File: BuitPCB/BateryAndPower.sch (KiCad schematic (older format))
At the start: 12 parts, among them J13 Conn_01x02, U5 STBC08

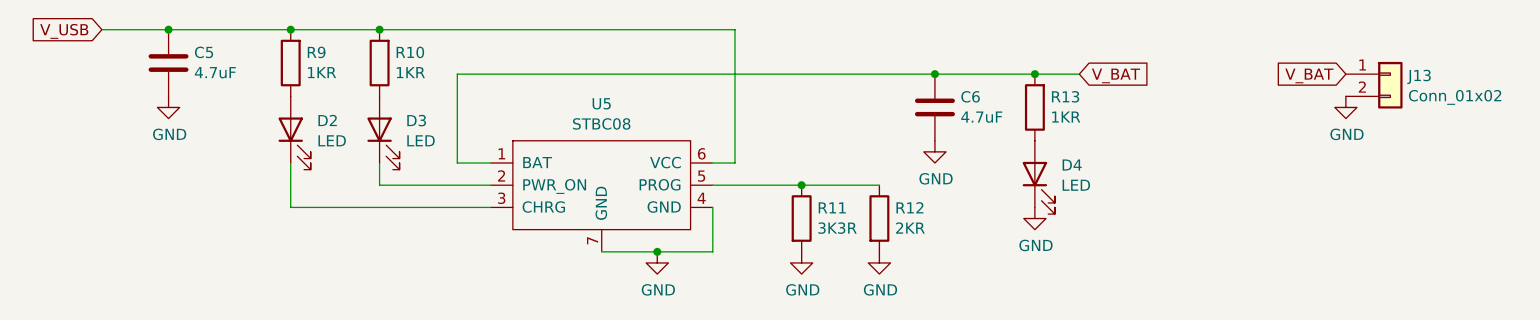
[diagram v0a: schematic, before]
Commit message: Updated adding esp8266 transceiver module
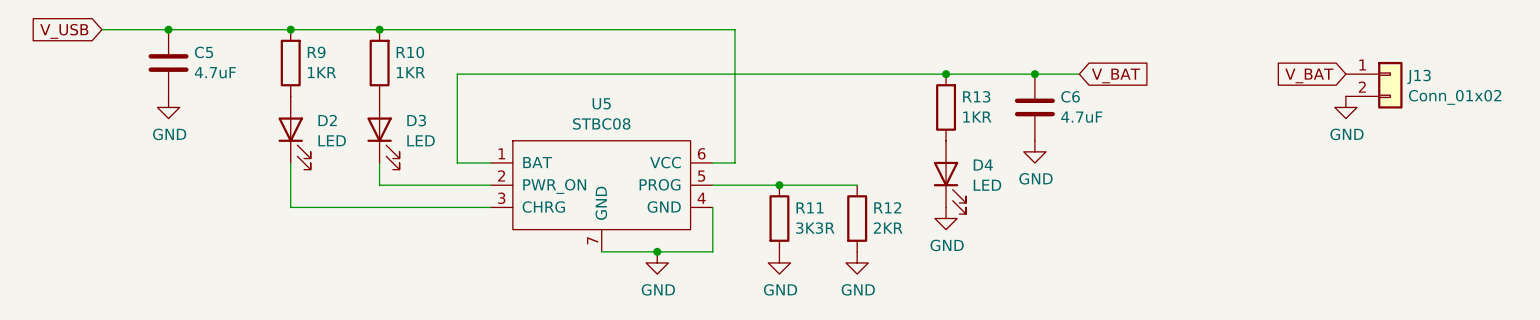
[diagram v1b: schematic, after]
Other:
- moved on the sheet: C6, D4, R11, R12, R13
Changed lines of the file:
@@
 L Device:R R11
 U 1 1 61BB77AB
-P 6600 4050
-F 0 "R11" H 6670 4096 50  0000 L CNN
-F 1 "3K3R" H 6670 4005 50  0000 L CNN
-F 2 "Resistor_SMD:R_0805_2012Metric_Pad1.20x1.40mm_HandSolder" V 6530 4050 50  0001 C CNN
-F 3 "~" H 6600 4050 50  0001 C CNN
-	1    6600 4050
+P 6500 4050
+F 0 "R11" H 6570 4096 50  0000 L CNN
+F 1 "3K3R" H 6570 4005 50  0000 L CNN
+F 2 "Resistor_SMD:R_0805_2012Metric_Pad1.20x1.40mm_HandSolder" V 6430 4050 50  0001 C CNN
+F 3 "~" H 6500 4050 50  0001 C CNN
+	1    6500 4050
 	1    0    0    -1
 $EndComp
@@
 L power:GND #PWR015
 U 1 1 61BB8030
-P 6600 4200
-F 0 "#PWR015" H 6600 3950 50  0001 C CNN
-F 1 "GND" H 6605 4027 50  0000 C CNN
-F 2 "" H 6600 4200 50  0001 C CNN
-F 3 "" H 6600 4200 50  0001 C CNN
-	1    6600 4200
-	1    0    0    -1
-$EndComp
-Wire Wire Line
-	6600 3900 6200 3900
+P 6500 4200
+F 0 "#PWR015" H 6500 3950 50  0001 C CNN
+F 1 "GND" H 6505 4027 50  0000 C CNN
+F 2 "" H 6500 4200 50  0001 C CNN
+F 3 "" H 6500 4200 50  0001 C CNN
+	1    6500 4200
+	1    0    0    -1
+$EndComp
 $Comp
 L Device:LED D2
@@
 Wire Wire Line
 	4300 4000 4300 3800
-Wire Wire Line
-	3750 3200 4300 3200
 Connection ~ 4300 3200
 Wire Wire Line
@@
 L Device:C C6
 U 1 1 61BC0B08
-P 7200 3550
-F 0 "C6" H 7315 3596 50  0000 L CNN
-F 1 "4.7uF" H 7315 3505 50  0000 L CNN
-F 2 "Capacitor_SMD:C_0805_2012Metric_Pad1.18x1.45mm_HandSolder" H 7238 3400 50  0001 C CNN
-F 3 "~" H 7200 3550 50  0001 C CNN
-	1    7200 3550
+P 7650 3550
+F 0 "C6" H 7765 3596 50  0000 L CNN
+F 1 "4.7uF" H 7765 3505 50  0000 L CNN
+F 2 "Capacitor_SMD:C_0805_2012Metric_Pad1.18x1.45mm_HandSolder" H 7688 3400 50  0001 C CNN
+F 3 "~" H 7650 3550 50  0001 C CNN
+	1    7650 3550
 	1    0    0    -1
 $EndComp
@@
 L power:GND #PWR023
 U 1 1 61BC31C7
-P 7200 3700
-F 0 "#PWR023" H 7200 3450 50  0001 C CNN
-F 1 "GND" H 7205 3527 50  0000 C CNN
-F 2 "" H 7200 3700 50  0001 C CNN
-F 3 "" H 7200 3700 50  0001 C CNN
-	1    7200 3700
+P 7650 3700
+F 0 "#PWR023" H 7650 3450 50  0001 C CNN
+F 1 "GND" H 7655 3527 50  0000 C CNN
+F 2 "" H 7650 3700 50  0001 C CNN
+F 3 "" H 7650 3700 50  0001 C CNN
+	1    7650 3700
 	1    0    0    -1
 $EndComp
@@
 L Device:R R12
 U 1 1 61BC63B7
-P 6950 4050
-F 0 "R12" H 7020 4096 50  0000 L CNN
-F 1 "2KR" H 7020 4005 50  0000 L CNN
-F 2 "Resistor_SMD:R_0805_2012Metric_Pad1.20x1.40mm_HandSolder" V 6880 4050 50  0001 C CNN
-F 3 "~" H 6950 4050 50  0001 C CNN
-	1    6950 4050
+P 6850 4050
+F 0 "R12" H 6920 4096 50  0000 L CNN
+F 1 "2KR" H 6920 4005 50  0000 L CNN
+F 2 "Resistor_SMD:R_0805_2012Metric_Pad1.20x1.40mm_HandSolder" V 6780 4050 50  0001 C CNN
+F 3 "~" H 6850 4050 50  0001 C CNN
+	1    6850 4050
 	1    0    0    -1
 $EndComp
@@
 L power:GND #PWR022
 U 1 1 61BC6606
-P 6950 4200
-F 0 "#PWR022" H 6950 3950 50  0001 C CNN
-F 1 "GND" H 6955 4027 50  0000 C CNN
-F 2 "" H 6950 4200 50  0001 C CNN
-F 3 "" H 6950 4200 50  0001 C CNN
-	1    6950 4200
-	1    0    0    -1
-$EndComp
-Wire Wire Line
-	6600 3900 6950 3900
-Connection ~ 6600 3900
-Wire Wire Line
-	5050 3400 7200 3400
+P 6850 4200
+F 0 "#PWR022" H 6850 3950 50  0001 C CNN
+F 1 "GND" H 6855 4027 50  0000 C CNN
+F 2 "" H 6850 4200 50  0001 C CNN
+F 3 "" H 6850 4200 50  0001 C CNN
+	1    6850 4200
+	1    0    0    -1
+$EndComp
 Wire Wire Line
 	5050 3400 5050 3800
@@
 Text GLabel 7850 3400 2    50   Input ~ 0
 V_BAT
-Connection ~ 7200 3400
-Wire Wire Line
-	3450 3200 3750 3200
-Connection ~ 3750 3200
 $Comp
 L Device:LED D4
 U 1 1 61BCC4CB
-P 7650 3850
-F 0 "D4" V 7689 3732 50  0000 R CNN
-F 1 "LED" V 7598 3732 50  0000 R CNN
-F 2 "LED_SMD:LED_0805_2012Metric" H 7650 3850 50  0001 C CNN
-F 3 "~" H 7650 3850 50  0001 C CNN
-	1    7650 3850
+P 7250 3850
+F 0 "D4" V 7289 3732 50  0000 R CNN
+F 1 "LED" V 7198 3732 50  0000 R CNN
+F 2 "LED_SMD:LED_0805_2012Metric" H 7250 3850 50  0001 C CNN
+F 3 "~" H 7250 3850 50  0001 C CNN
+	1    7250 3850
 	0    -1   -1   0
 $EndComp
@@
 L Device:R R13
 U 1 1 61BCC4D1
-P 7650 3550
-F 0 "R13" H 7580 3504 50  0000 R CNN
-F 1 "1KR" H 7580 3595 50  0000 R CNN
-F 2 "Resistor_SMD:R_0805_2012Metric_Pad1.20x1.40mm_HandSolder" V 7580 3550 50  0001 C CNN
-F 3 "~" H 7650 3550 50  0001 C CNN
-	1    7650 3550
+P 7250 3550
+F 0 "R13" H 7180 3504 50  0000 R CNN
+F 1 "1KR" H 7180 3595 50  0000 R CNN
+F 2 "Resistor_SMD:R_0805_2012Metric_Pad1.20x1.40mm_HandSolder" V 7180 3550 50  0001 C CNN
+F 3 "~" H 7250 3550 50  0001 C CNN
+	1    7250 3550
 	-1   0    0    1
 $EndComp
-Wire Wire Line
-	7200 3400 7650 3400
-Connection ~ 7650 3400
-Wire Wire Line
-	7650 3400 7850 3400
 $Comp
 L power:GND #PWR030
 U 1 1 61BCD5D7
-P 7650 4000
-F 0 "#PWR030" H 7650 3750 50  0001 C CNN
-F 1 "GND" H 7655 3827 50  0000 C CNN
-F 2 "" H 7650 4000 50  0001 C CNN
-F 3 "" H 7650 4000 50  0001 C CNN
-	1    7650 4000
+P 7250 4000
+F 0 "#PWR030" H 7250 3750 50  0001 C CNN
+F 1 "GND" H 7255 3827 50  0000 C CNN
+F 2 "" H 7250 4000 50  0001 C CNN
+F 3 "" H 7250 4000 50  0001 C CNN
+	1    7250 4000
 	1    0    0    -1
 $EndComp
@@
 	1    0    0    -1
 $EndComp
+Connection ~ 7650 3400
+Wire Wire Line
+	7650 3400 7850 3400
+Wire Wire Line
+	5050 3400 7250 3400
+Connection ~ 7250 3400
+Wire Wire Line
+	7250 3400 7650 3400
+Connection ~ 3750 3200
+Wire Wire Line
+	3750 3200 4300 3200
+Wire Wire Line
+	3450 3200 3750 3200
+Connection ~ 6500 3900
+Wire Wire Line
+	6500 3900 6200 3900
+Wire Wire Line
+	6500 3900 6850 3900
 $EndSCHEMATC

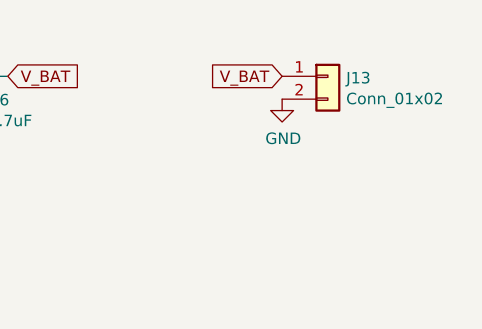
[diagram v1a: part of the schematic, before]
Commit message: Updated to almost every component and started routing
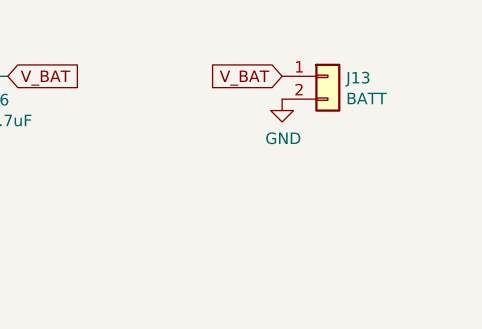
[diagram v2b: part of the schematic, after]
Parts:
- J13: value Conn_01x02 -> BATT
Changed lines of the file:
@@
 P 9250 3400
 F 0 "J13" H 9330 3392 50  0000 L CNN
-F 1 "Conn_01x02" H 9330 3301 50  0000 L CNN
+F 1 "BATT" H 9330 3301 50  0000 L CNN
 F 2 "Connector_JST:JST_PH_S2B-PH-SM4-TB_1x02-1MP_P2.00mm_Horizontal" H 9250 3400 50  0001 C CNN
 F 3 "~" H 9250 3400 50  0001 C CNN
